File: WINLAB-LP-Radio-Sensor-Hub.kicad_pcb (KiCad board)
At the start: 2 copper layers, 65 x 53 mm, 73 parts, among them IC1 TLV74033PDBVR, J1 FTSH-105-01-L-DV-K-A, J2 Conn_Coaxial, J3 Conn_Coaxial, J4 USB_C_Receptacle_USB2.0_16P, J5 Conn_01x05, J6 Conn_01x05, J7 Conn_01x05, J8 Conn_01x05, J9 Conn_01x02, Q1 AO3401A, Q2 AO3401A, U1 EFR32FG23L020F128GM40-C, U2 Si7021-A20, U3 CH340N, U4 CN3063, U5 TPS7A0522PDBV, U6 ADG902BRMZ, Y1 39MHz 10pF

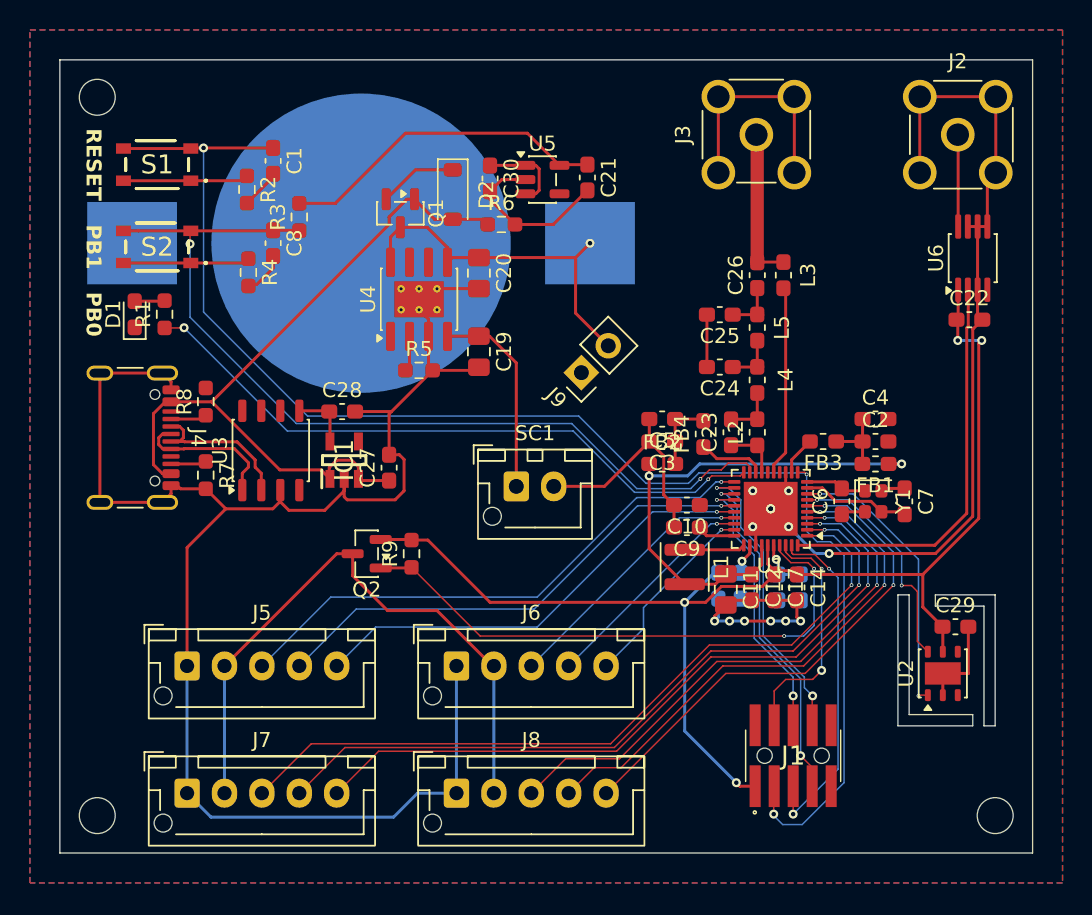
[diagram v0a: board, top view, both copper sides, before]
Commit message: completed layout and routing with preliminary matching network
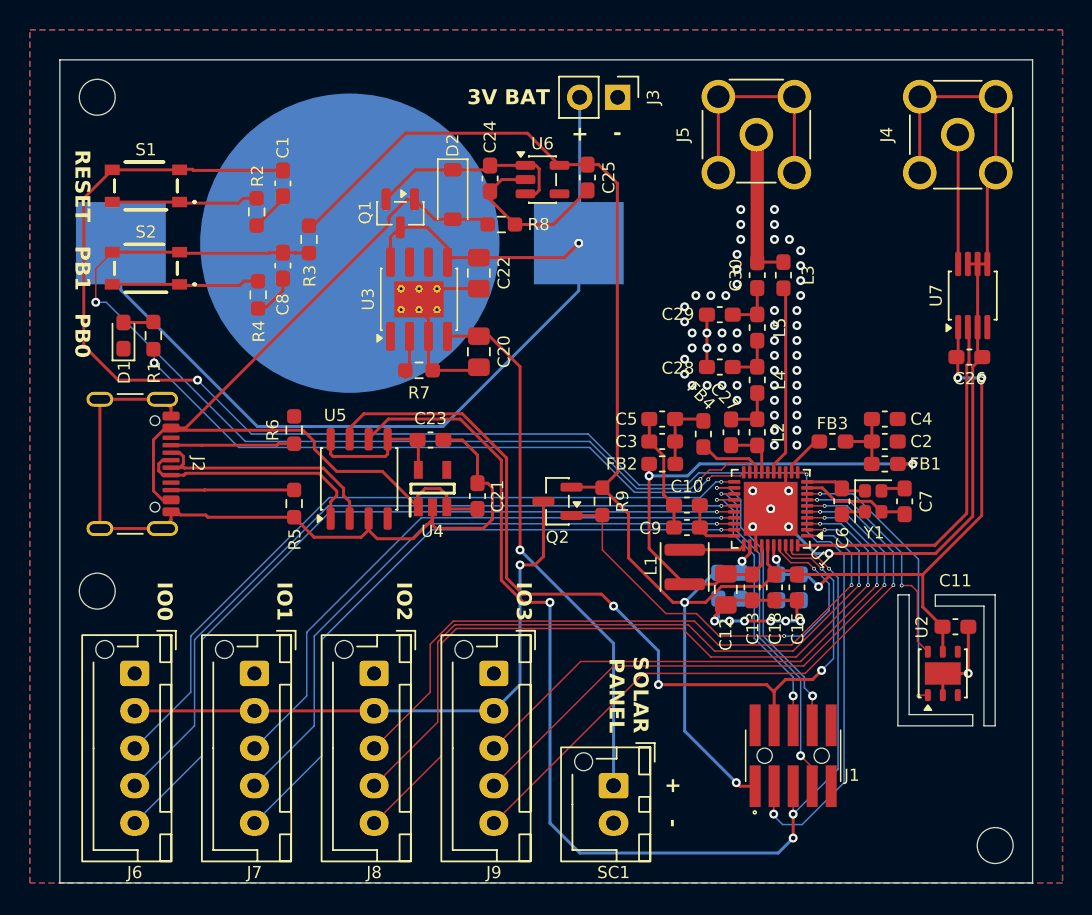
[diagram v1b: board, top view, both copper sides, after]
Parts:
- moved SC1 21.0 mm to (221.0, 77.5), turned to -90 degrees
- moved J3 18.6 mm to (221.3, 31.5), turned to -90 degrees
- moved J8 14.8 mm to (205.0, 70.0), turned to -90 degrees
- moved J7 13.5 mm to (197.0, 70.0), turned to -90 degrees
- moved Q2 13.2 mm to (217.2, 58.5)
- moved R9 13.2 mm to (220.2, 58.5)
- moved J9 8.38 mm to (213.0, 70.0), turned to -90 degrees
- moved C21 6.20 mm to (211.9, 58.1)
- moved C23 6.20 mm to (208.8, 54.4)
- moved R5 6.20 mm to (199.7, 58.6)
- moved R6 6.20 mm to (199.7, 53.7)
- moved U4 6.20 mm to (208.9, 57.6)
- moved U5 6.20 mm to (204.0, 57.0)
- moved J6 3.54 mm to (189.0, 70.0), turned to -90 degrees
- moved C26 2.50 mm to (244.8, 48.9)
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- renumbered C29 to C11, C11 to C12, C12 to C13, C13 to C14, C14 to C15, C15 to C16, C16 to C17, C17 to C18, C18 to C19, C19 to C20, C27 to C21, C20 to C22, C28 to C23, C30 to C24, C21 to C25, C22 to C26, C23 to C27, C24 to C28, C25 to C29, C26 to C30, J4 to J2, J9 to J3, J2 to J4, J3 to J5, J5 to J6, J6 to J7, J7 to J8, J8 to J9, R7 to R5, R8 to R6, R5 to R7, R6 to R8, U4 to U3, IC1 to U4, U3 to U5, U5 to U6, U6 to U7
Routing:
- net VCOM_TX: track 23.2 -> 79.5 mm, vias 2 -> 4
- net GND: track 250.6 -> 196.4 mm, vias 13 -> 67
- net V_BAT: track 24.1 -> 70.8 mm
- net VCOM_RX: track 16.1 -> 60.0 mm, vias 2 -> 4
- net IO1_2: track 13.2 -> 44.7 mm
- net IO1_1: track 15.0 -> 42.8 mm
- net IO1_0: track 17.7 -> 40.9 mm
- net V_SOLAR: track 13.6 -> 36.3 mm, vias 0 -> 1
- net IO0_2: track 30.8 -> 53.2 mm
- net IO0_1: track 33.5 -> 51.2 mm
- net +V_SYS: track 115.8 -> 130.3 mm, vias 6 -> 7
- net IO0_0: track 36.7 -> 49.6 mm
- net RESET: track 97.3 -> 107.4 mm
- net BTN_USR: track 60.9 -> 71.0 mm
- net V_USB: track 50.1 -> 59.8 mm
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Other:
- board size 65 x 53 mm -> 65 x 55 mm
- board text added: "+"
- board text added: "-"
- board text added: "3V BAT"
- board text added: "IO0"
- board text added: "IO1"
- board text added: "IO2"
- board text added: "IO3"
- board text added: "SOLAR PANEL"

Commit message: minor layout and silkscreen tweaks
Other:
- board text added: "ACTIVE RF"
- board text added: "BACKSCATTER"

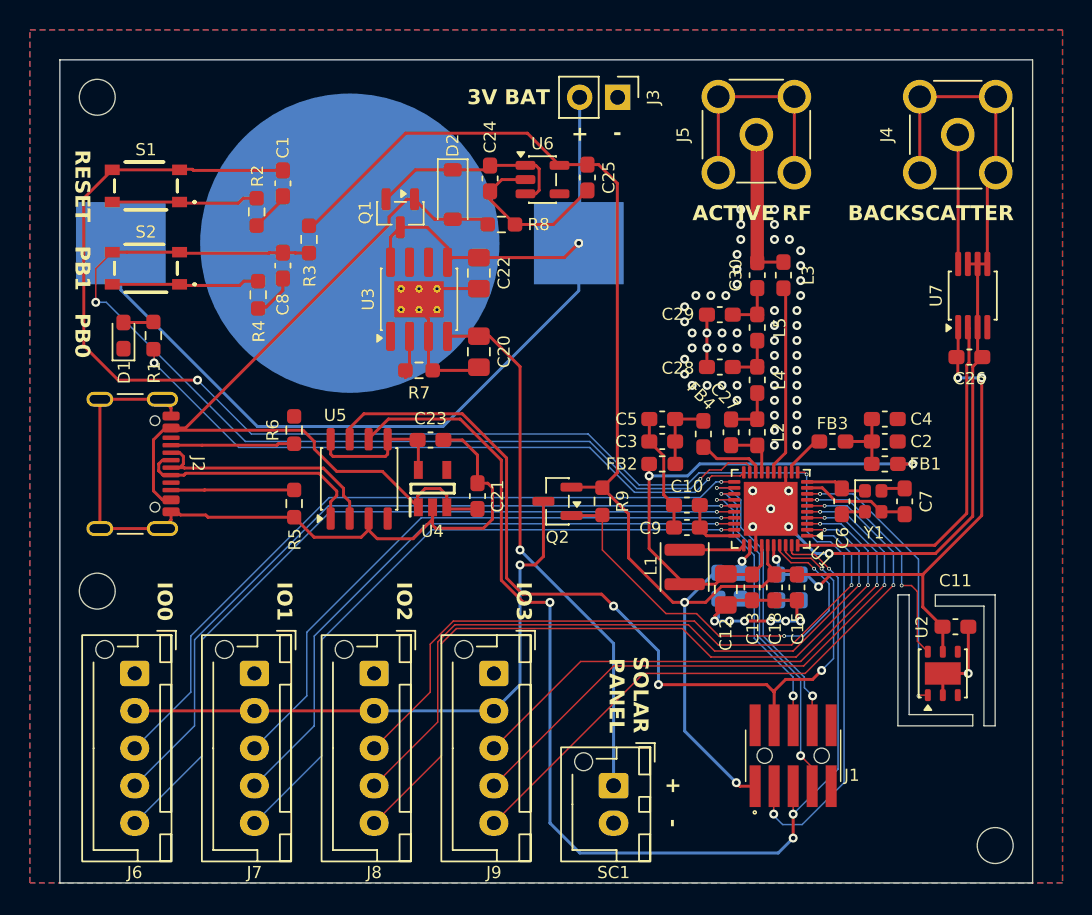
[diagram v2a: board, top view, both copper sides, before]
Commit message: switch to 0402 matching network closer to reference design
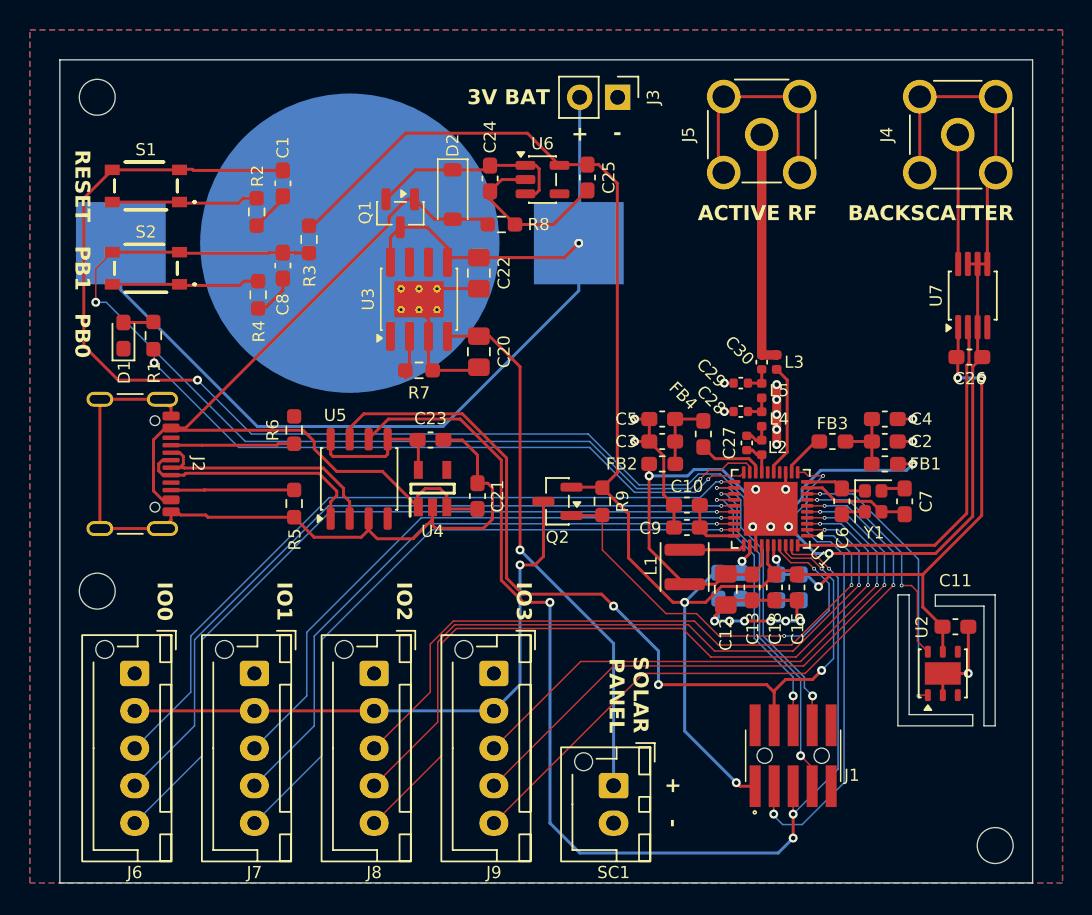
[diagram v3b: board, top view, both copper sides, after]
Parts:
- C27, C28, C29, C30: footprint Capacitor_SMD:C_0603_1608Metric_Pad1.08x0.95mm_HandSolder -> Capacitor_SMD:C_0402_1005Metric
- L2, L3, L4, L5: footprint Inductor_SMD:L_0603_1608Metric_Pad1.05x0.95mm_HandSolder -> Inductor_SMD:L_0402_1005Metric
- moved L3 5.83 mm to (231.9, 49.2)
- moved C30 5.82 mm to (230.9, 49.2)
- moved C29 4.78 mm to (229.5, 50.6)
- moved L5 4.22 mm to (230.9, 51.1)
- moved C28 3.29 mm to (229.5, 52.5)
- moved L4 2.63 mm to (230.9, 53.0)
- moved C27 1.27 mm to (229.9, 54.6)
- moved L2 1.06 mm to (230.9, 54.9)
- moved J5 0.36 mm to (230.9, 34.0)
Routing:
- net Net-(J5-In): track 10.3 -> 15.6 mm
- net RF_I: track 12.7 -> 7.54 mm
- net GND: track 196.4 -> 200.4 mm, vias 67 -> 24
- net RESET: track 107.4 -> 111.2 mm
- net EFR32_DCDC: track 34.3 -> 37.0 mm
- net Net-(C29-Pad1): track 3.41 -> 1.86 mm
- net Net-(C28-Pad1): track 3.39 -> 1.86 mm
- net Net-(C27-Pad2): track 3.51 -> 2.06 mm
- net RF_O: track 3.66 -> 2.30 mm
